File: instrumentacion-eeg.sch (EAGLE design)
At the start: 39 parts, among them IC1 LMV321AIDCKR, IC15 LMV321AIDCKR, IC16 LMV321AIDCKR, IC2 ESP32-S3-WROOM-1-N4R2, IC3 LMV321AIDCKR, IC5 MCP73831T-2ACI_OT, IC7 AD8226ARZ, IC9 LP38692MP-3.3_NOPB, J1 USB3500-30-A-KIT, J3 SJ-3523-SMT-TR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

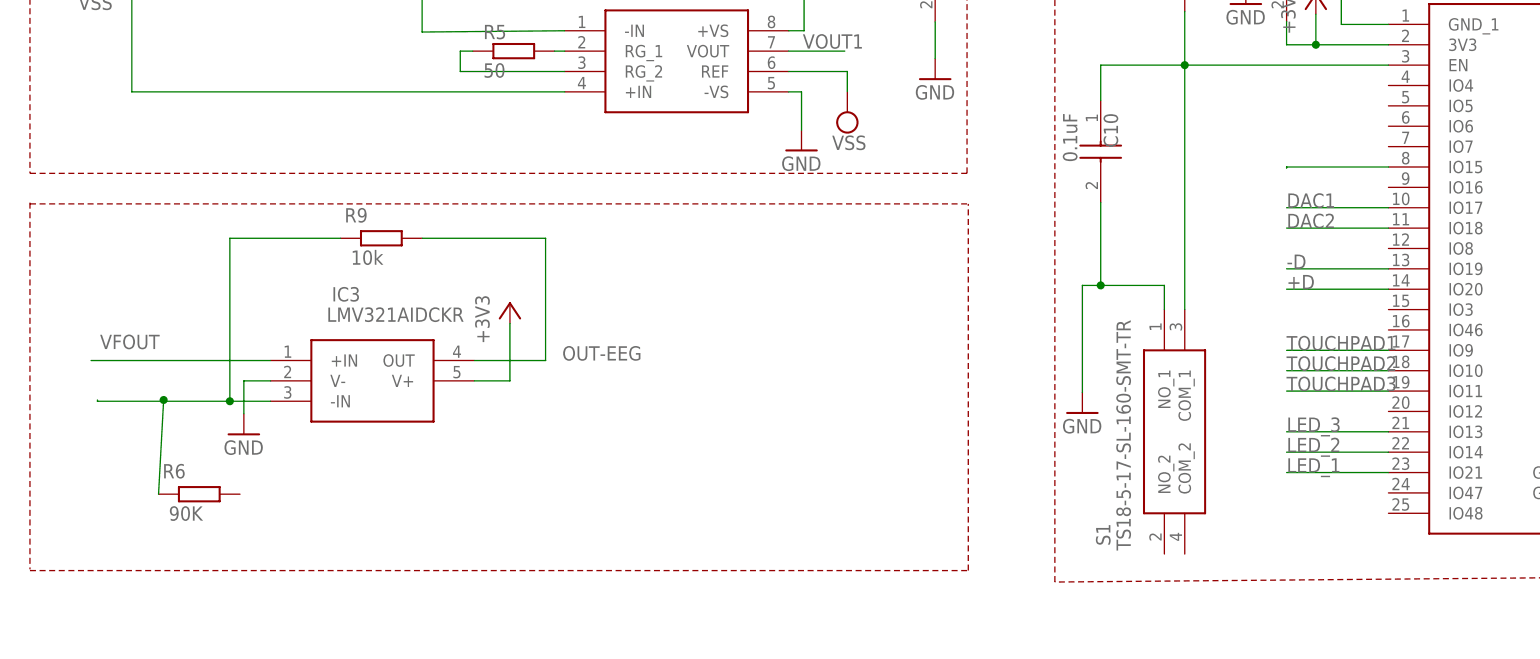
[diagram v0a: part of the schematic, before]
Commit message: Agrego correccion de amplificador
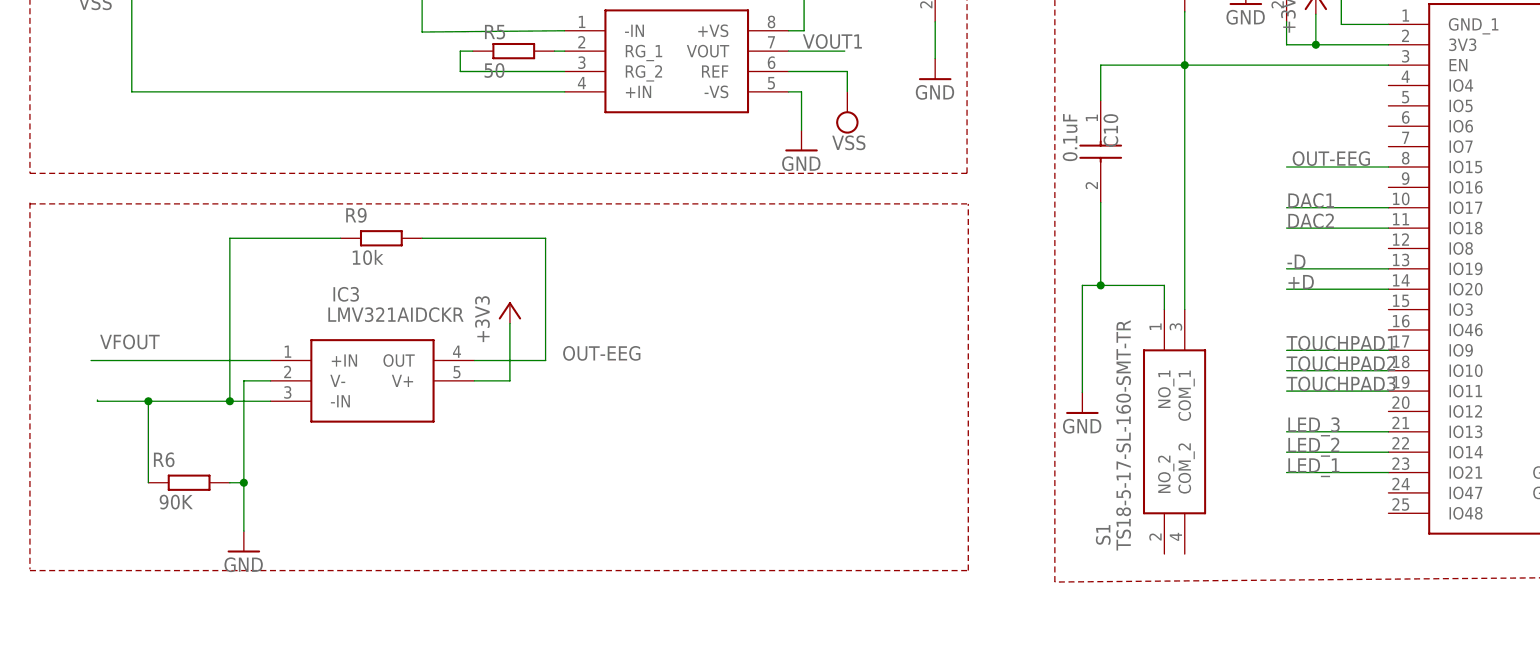
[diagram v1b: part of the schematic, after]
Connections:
- removed net N$8: IC2.IO15
- net GND: now also R6.2
- net OUT-EEG: now also IC2.IO15
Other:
- moved on the sheet: R6
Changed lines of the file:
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@@
 <attribute name="VALUE" x="54.76875" y="-79.6925" size="1.778" layer="96" rot="R90"/>
 </instance>
-<instance part="R6" gate="G$1" x="18.57375" y="-98.425" smashed="yes">
-<attribute name="NAME" x="13.97" y="-96.45015" size="1.778" layer="95"/>
-<attribute name="VALUE" x="14.76375" y="-101.727" size="1.778" layer="96"/>
+<instance part="R6" gate="G$1" x="17.30375" y="-96.99625" smashed="yes">
+<attribute name="NAME" x="12.7" y="-95.0214" size="1.778" layer="95"/>
+<attribute name="VALUE" x="13.49375" y="-100.29825" size="1.778" layer="96"/>
 </instance>
-<instance part="GND16" gate="1" x="24.13" y="-90.96375" smashed="yes">
-<attribute name="VALUE" x="21.59" y="-93.50375" size="1.778" layer="96"/>
+<instance part="GND16" gate="1" x="24.13" y="-105.56875" smashed="yes">
+<attribute name="VALUE" x="21.59" y="-108.10875" size="1.778" layer="96"/>
 </instance>
 <instance part="R9" gate="G$1" x="41.275" y="-66.51625" smashed="yes">
@@
 <wire x1="24.13" y1="-84.29625" x2="27.46375" y2="-84.29625" width="0.1524" layer="91"/>
 <pinref part="GND16" gate="1" pin="GND"/>
-<wire x1="24.13" y1="-84.29625" x2="24.13" y2="-88.42375" width="0.1524" layer="91"/>
+<wire x1="24.13" y1="-84.29625" x2="24.13" y2="-96.99625" width="0.1524" layer="91"/>
+<pinref part="R6" gate="G$1" pin="2"/>
+<wire x1="24.13" y1="-96.99625" x2="24.13" y2="-103.02875" width="0.1524" layer="91"/>
+<wire x1="22.38375" y1="-96.99625" x2="24.13" y2="-96.99625" width="0.1524" layer="91"/>
+<junction x="24.13" y="-96.99625"/>
 </segment>
 </net>
@@
 <segment>
 <pinref part="R6" gate="G$1" pin="1"/>
-<wire x1="13.49375" y1="-98.425" x2="14.12875" y2="-86.6775" width="0.1524" layer="91"/>
-<junction x="14.12875" y="-86.6775"/>
-<wire x1="14.12875" y1="-86.6775" x2="14.12875" y2="-86.83625" width="0.1524" layer="91"/>
+<wire x1="12.22375" y1="-96.99625" x2="12.22375" y2="-86.83625" width="0.1524" layer="91"/>
+<junction x="12.22375" y="-86.83625"/>
 </segment>
 </net>
@@
 <label x="63.8175" y="-81.75625" size="1.778" layer="95"/>
 </segment>
-</net>
-<net name="N$8" class="0">
 <segment>
 <pinref part="IC2" gate="G$1" pin="IO15"/>
 <wire x1="166.84625" y1="-57.62625" x2="154.14625" y2="-57.62625" width="0.1524" layer="91"/>
-<wire x1="154.14625" y1="-57.62625" x2="154.14625" y2="-57.785" width="0.1524" layer="91"/>
-</segment>
-</net>
+<label x="154.78125" y="-57.4675" size="1.778" layer="95"/>
+</segment>
+</net>

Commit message: Agrego archivos
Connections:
- removed net N$15: IC3.+IN
- removed net N$7: R6.1
- net N$14: now also R6.1
- net VFOUT: now also IC3.+IN
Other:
- note removed: "VFOUT"
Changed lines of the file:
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@@
 <wire x1="114.45875" y1="-107.95" x2="114.45875" y2="-62.23" width="0.1524" layer="94" style="shortdash"/>
 <wire x1="-2.54" y1="-107.95" x2="114.3" y2="-107.95" width="0.1524" layer="94" style="shortdash"/>
-<text x="6.19125" y="-80.3275" size="1.778" layer="95">VFOUT</text>
 </plain>
 <instances>
@@
 <attribute name="NAME" x="54.19725" y="90.58275" size="1.778" layer="95" rot="R180"/>
 <attribute name="VALUE" x="55.14975" y="92.17025" size="1.778" layer="96" rot="R180"/>
-<attribute name="POPULARITY" x="56.67375" y="87.47125" size="1.778" layer="96" rot="R180"/>
+<attribute name="POPULARITY" x="55.08625" y="85.725" size="1.778" layer="96" rot="R180"/>
 </instance>
 <instance part="C5" gate="G$1" x="102.39375" y="91.59875" smashed="yes" rot="R180">
@@
 <wire x1="187.6425" y1="79.375" x2="187.6425" y2="71.755" width="0.1524" layer="91"/>
 <pinref part="IC9" gate="G$1" pin="EN"/>
-<wire x1="187.6425" y1="71.755" x2="187.6425" y2="66.51625" width="0.1524" layer="91"/>
+<wire x1="187.6425" y1="71.755" x2="187.6425" y2="66.19875" width="0.1524" layer="91"/>
 <wire x1="187.6425" y1="79.375" x2="191.77" y2="79.375" width="0.1524" layer="91"/>
 <pinref part="S3" gate="G$1" pin="COM"/>
 <wire x1="156.5275" y1="75.2475" x2="142.875" y2="75.2475" width="0.1524" layer="91"/>
-<wire x1="142.875" y1="75.2475" x2="142.875" y2="66.51625" width="0.1524" layer="91"/>
-<wire x1="142.875" y1="66.51625" x2="187.6425" y2="66.51625" width="0.1524" layer="91"/>
+<wire x1="142.875" y1="75.2475" x2="142.875" y2="66.19875" width="0.1524" layer="91"/>
+<wire x1="142.875" y1="66.19875" x2="187.6425" y2="66.19875" width="0.1524" layer="91"/>
 <pinref part="IC9" gate="G$1" pin="IN"/>
 <wire x1="191.77" y1="71.755" x2="187.6425" y2="71.755" width="0.1524" layer="91"/>
@@
 <label x="228.12375" y="25.24125" size="1.778" layer="95"/>
 </segment>
+<segment>
+<pinref part="IC3" gate="G$1" pin="+IN"/>
+<wire x1="27.46375" y1="-81.75625" x2="16.66875" y2="-81.75625" width="0.1524" layer="91"/>
+<label x="16.8275" y="-81.5975" size="1.778" layer="95"/>
+</segment>
 </net>
 <net name="N$2" class="0">
@@
 </segment>
 </net>
-<net name="N$7" class="0">
-<segment>
-<pinref part="R6" gate="G$1" pin="1"/>
-<wire x1="12.22375" y1="-96.99625" x2="12.22375" y2="-86.83625" width="0.1524" layer="91"/>
-<junction x="12.22375" y="-86.83625"/>
-</segment>
-</net>
 <net name="N$14" class="0">
 <segment>
+<pinref part="R9" gate="G$1" pin="1"/>
 <wire x1="22.38375" y1="-86.83625" x2="22.38375" y2="-66.51625" width="0.1524" layer="91"/>
-<pinref part="R9" gate="G$1" pin="1"/>
 <wire x1="22.38375" y1="-66.51625" x2="36.195" y2="-66.51625" width="0.1524" layer="91"/>
 <pinref part="IC3" gate="G$1" pin="-IN"/>
 <wire x1="27.46375" y1="-86.83625" x2="22.38375" y2="-86.83625" width="0.1524" layer="91"/>
-<wire x1="22.38375" y1="-86.83625" x2="5.87375" y2="-86.83625" width="0.1524" layer="91"/>
-<wire x1="5.87375" y1="-86.83625" x2="5.87375" y2="-86.6775" width="0.1524" layer="91"/>
+<pinref part="R6" gate="G$1" pin="1"/>
+<wire x1="12.22375" y1="-96.99625" x2="12.22375" y2="-86.83625" width="0.1524" layer="91"/>
+<wire x1="12.22375" y1="-86.83625" x2="22.38375" y2="-86.83625" width="0.1524" layer="91"/>
 <junction x="22.38375" y="-86.83625"/>
-</segment>
-</net>
-<net name="N$15" class="0">
-<segment>
-<pinref part="IC3" gate="G$1" pin="+IN"/>
-<wire x1="27.46375" y1="-81.75625" x2="5.08" y2="-81.75625" width="0.1524" layer="91"/>
+<wire x1="22.38375" y1="-86.83625" x2="27.46375" y2="-86.83625" width="0.1524" layer="91"/>
 </segment>
 </net>
@@
 </segment>
 </net>
+<net name="N$8" class="0">
+<segment>
+<wire x1="5.87375" y1="-86.83625" x2="5.87375" y2="-86.6775" width="0.1524" layer="91"/>
+</segment>
+</net>
